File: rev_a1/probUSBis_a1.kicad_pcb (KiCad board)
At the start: 2 copper layers, 23 parts, among them CON1 USB-MINI-B, IC1 ATTINY85-P, P1 USB_A_MALE, P2 CONN_8, P3 CONN_4, U1 LM78L05ACZ

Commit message: made some changes to pcb, added cut edge
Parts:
- moved D4 25.0 mm to (141.0, 111.8), turned to 0 degrees
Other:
- board outline added: 44.5 x 22.9 mm
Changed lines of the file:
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@@
     (links 52)
     (no_connects 52)
-    (area 0 0 0 0)
+    (area 93.996934 87.477599 151.13127 115.23345)
     (thickness 1.6)
-    (drawings 0)
+    (drawings 4)
     (tracks 0)
     (zones 0)
@@
   )
   (module D3 (layer F.Cu)
-    (at 130.81 88.9 180)
+    (at 140.97 111.76)
     (descr "Diode 3 pas")
     (tags "DIODE DEV")
-    (fp_text reference D4 (at 0 0 180) (layer F.SilkS)
-      (effects (font (size 1.016 1.016) (thickness 0.2032)))
-    )
-    (fp_text value DIODE (at 0 0 180) (layer F.SilkS) hide
+    (fp_text reference D4 (at 0 0) (layer F.SilkS)
+      (effects (font (size 1.016 1.016) (thickness 0.2032)))
+    )
+    (fp_text value DIODE (at 0 0) (layer F.SilkS) hide
       (effects (font (size 1.016 1.016) (thickness 0.2032)))
     )
@@
     (fp_line (start 2.54 -1.016) (end 2.54 1.016) (layer F.SilkS) (width 0.3048))
     (fp_line (start 2.286 1.016) (end 2.286 -1.016) (layer F.SilkS) (width 0.3048))
-    (pad 2 thru_hole rect (at 3.81 0 180) (size 1.397 1.397) (drill 0.8128)
+    (pad 2 thru_hole rect (at 3.81 0) (size 1.397 1.397) (drill 0.8128)
       (layers *.Cu *.Mask F.SilkS)
       (net 2 +5V)
     )
-    (pad 1 thru_hole circle (at -3.81 0 180) (size 1.397 1.397) (drill 0.8128)
+    (pad 1 thru_hole circle (at -3.81 0) (size 1.397 1.397) (drill 0.8128)
       (layers *.Cu *.Mask F.SilkS)
       (net 8 N-0000016)
@@
     )
   )
+  (gr_line (start 149.86 91.44) (end 105.41 91.44) (angle 90) (layer Edge.Cuts) (width 0.1))
+  (gr_line (start 149.86 114.3) (end 149.86 91.44) (angle 90) (layer Edge.Cuts) (width 0.1))
+  (gr_line (start 105.41 114.3) (end 149.86 114.3) (angle 90) (layer Edge.Cuts) (width 0.1))
+  (gr_line (start 105.41 91.44) (end 105.41 114.3) (angle 90) (layer Edge.Cuts) (width 0.1))
 )

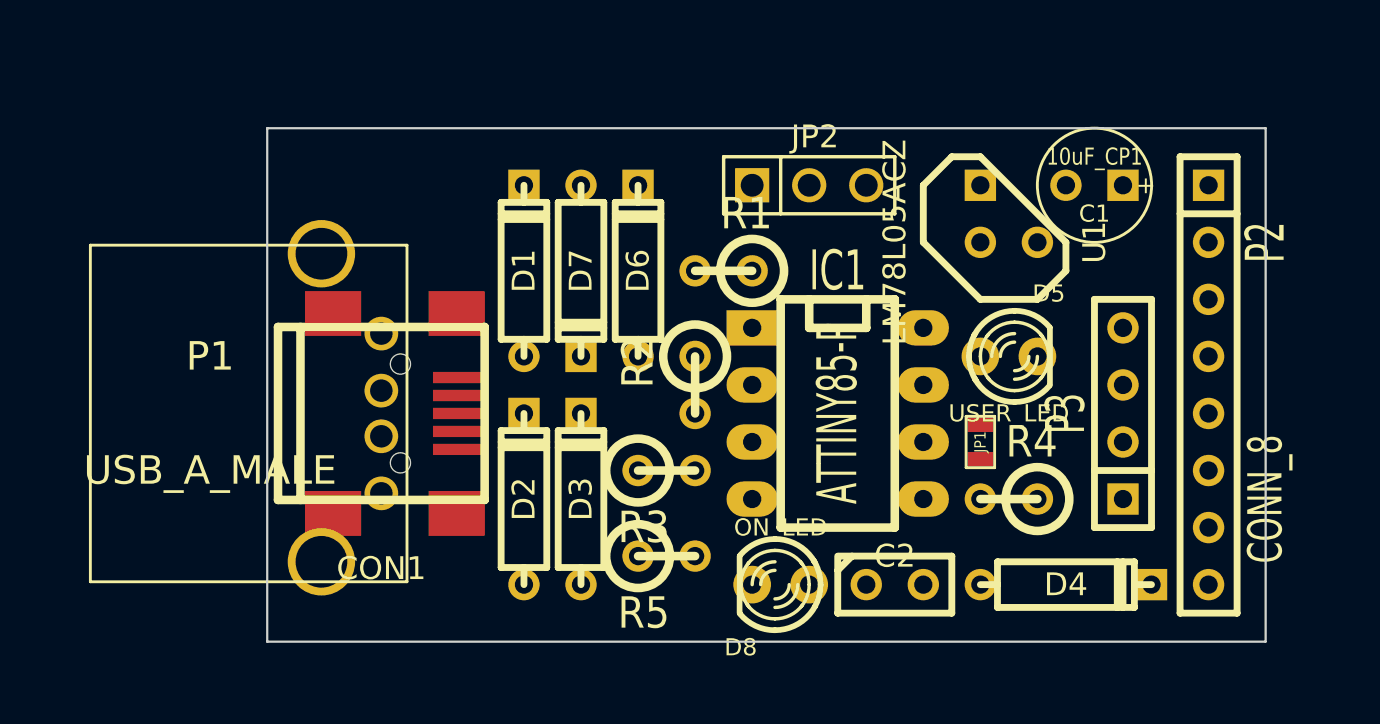
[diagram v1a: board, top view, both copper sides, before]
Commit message: made dsn, also making pin labels
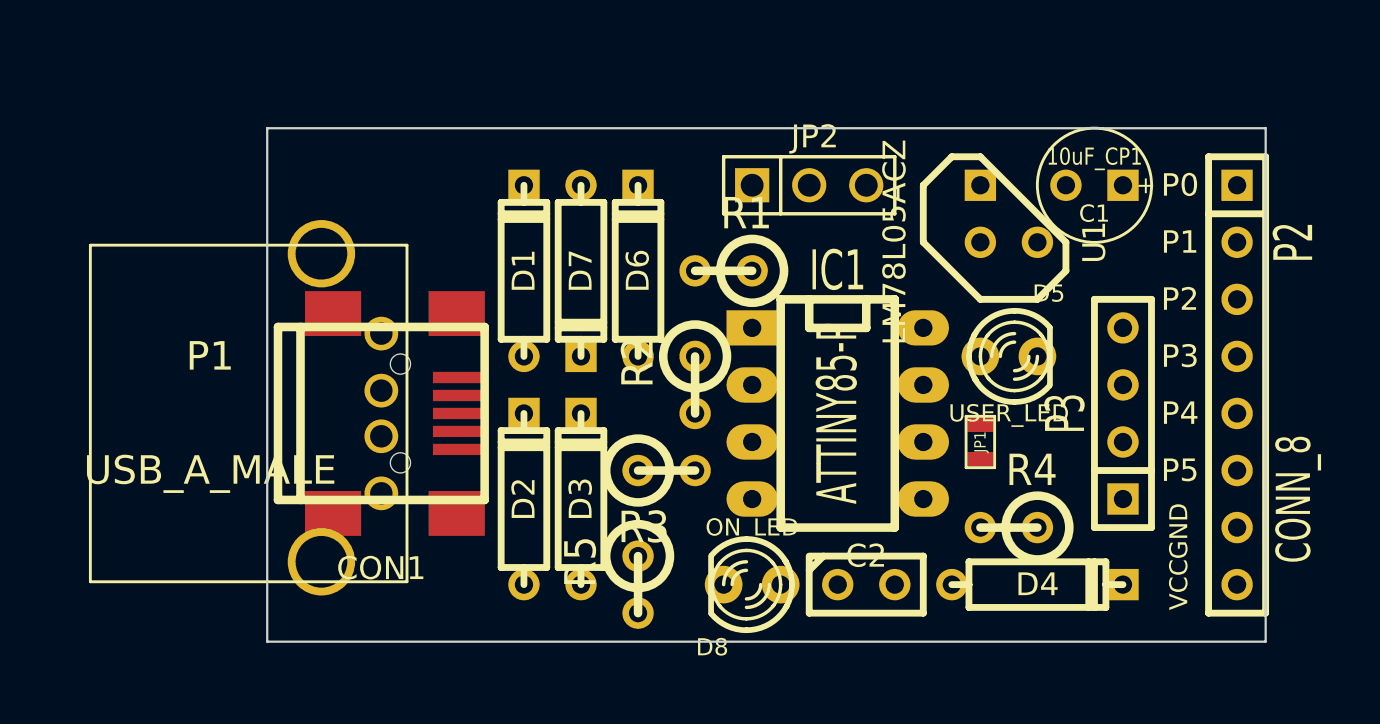
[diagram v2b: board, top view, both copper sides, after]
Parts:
- moved R5 1.80 mm to (121.9, 111.8), turned to 270 degrees
- moved D4 1.27 mm to (139.7, 111.8)
- moved D8 1.27 mm to (127.0, 111.8)
- moved P2 1.27 mm to (148.6, 102.9)
- moved R4 1.27 mm to (138.4, 109.2)
- moved C2 1.27 mm to (132.1, 111.8)
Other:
- board text added: "GND"
- board text added: "P0"
- board text added: "P1"
- board text added: "P2"
- board text added: "P3"
- board text added: "P4"
- board text added: "P5"
- board text added: "VCC"
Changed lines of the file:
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@@
     (links 52)
     (no_connects 52)
-    (area 93.996934 87.477599 151.13127 115.23345)
+    (area 93.996934 90.096623 152.40127 115.23345)
     (thickness 1.6)
-    (drawings 4)
+    (drawings 12)
     (tracks 0)
     (zones 0)
@@
   )
   (module C1 (layer F.Cu)
-    (at 133.35 111.76)
+    (at 132.08 111.76)
     (descr "Condensateur e = 1 pas")
     (tags C)
@@
   )
   (module D3 (layer F.Cu)
-    (at 140.97 111.76)
+    (at 139.7 111.76)
     (descr "Diode 3 pas")
     (tags "DIODE DEV")
@@
   )
   (module LED-3MM (layer F.Cu)
-    (at 128.27 111.76 180)
+    (at 127 111.76 180)
     (descr "LED 3mm - Lead pitch 100mil (2,54mm)")
     (tags "LED led 3mm 3MM 100mil 2,54mm")
@@
   )
   (module SIL-8 (layer F.Cu)
-    (at 147.32 102.87 270)
+    (at 148.59 102.87 270)
     (descr "Connecteur 8 pins")
     (tags "CONN DEV")
@@
   )
   (module R1 (layer F.Cu)
-    (at 138.43 107.95 180)
+    (at 138.43 109.22 180)
     (descr "Resistance verticale")
     (tags R)
@@
   )
   (module R1 (layer F.Cu)
-    (at 123.19 110.49)
+    (at 121.92 111.76 270)
     (descr "Resistance verticale")
     (tags R)
     (autoplace_cost90 10)
     (autoplace_cost180 10)
-    (fp_text reference R5 (at -1.016 2.54) (layer F.SilkS)
+    (fp_text reference R5 (at -1.016 2.54 270) (layer F.SilkS)
       (effects (font (size 1.397 1.27) (thickness 0.2032)))
     )
-    (fp_text value 1K_R (at -1.143 2.54) (layer F.SilkS) hide
+    (fp_text value 1K_R (at -1.143 2.54 270) (layer F.SilkS) hide
       (effects (font (size 1.397 1.27) (thickness 0.2032)))
     )
     (fp_line (start -1.27 0) (end 1.27 0) (layer F.SilkS) (width 0.381))
     (fp_circle (center -1.27 0) (end -0.635 1.27) (layer F.SilkS) (width 0.381))
-    (pad 1 thru_hole circle (at -1.27 0) (size 1.397 1.397) (drill 0.8128)
-      (layers *.Cu *.Mask F.SilkS)
-      (net 3 GND)
-    )
-    (pad 2 thru_hole circle (at 1.27 0) (size 1.397 1.397) (drill 0.8128)
+    (pad 1 thru_hole circle (at -1.27 0 270) (size 1.397 1.397) (drill 0.8128)
+      (layers *.Cu *.Mask F.SilkS)
+      (net 3 GND)
+    )
+    (pad 2 thru_hole circle (at 1.27 0 270) (size 1.397 1.397) (drill 0.8128)
       (layers *.Cu *.Mask F.SilkS)
       (net 18 N-000009)
@@
     )
   )
+  (gr_text VCC (at 146 111.76 90) (layer F.SilkS)
+    (effects (font (size 0.8 0.8) (thickness 0.1)))
+  )
+  (gr_text "   GND" (at 146 109.9 90) (layer F.SilkS)
+    (effects (font (size 0.8 0.8) (thickness 0.1)))
+  )
+  (gr_text P5 (at 146.05 106.68) (layer F.SilkS)
+    (effects (font (size 1 1) (thickness 0.25)))
+  )
+  (gr_text P4 (at 146.05 104.14) (layer F.SilkS)
+    (effects (font (size 1 1) (thickness 0.25)))
+  )
+  (gr_text P3 (at 146.05 101.6) (layer F.SilkS)
+    (effects (font (size 1 1) (thickness 0.25)))
+  )
+  (gr_text P1 (at 146.05 96.52) (layer F.SilkS)
+    (effects (font (size 1 1) (thickness 0.25)))
+  )
+  (gr_text P2 (at 146.05 99.06) (layer F.SilkS)
+    (effects (font (size 1 1) (thickness 0.25)))
+  )
+  (gr_text P0 (at 146.05 93.98) (layer F.SilkS)
+    (effects (font (size 1 1) (thickness 0.25)))
+  )
   (gr_line (start 149.86 91.44) (end 105.41 91.44) (angle 90) (layer Edge.Cuts) (width 0.1))

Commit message: editing pcb layout, trying to compress more
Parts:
- moved D4 17.0 mm to (130.5, 97.5), turned to 180 degrees
- moved R4 11.0 mm to (142.6, 99.1), turned to 90 degrees
- moved P3 8.52 mm to (139.7, 111.8), turned to 0 degrees
- moved P1 2.64 mm to (111.2, 106.7)
- moved JP2 2.54 mm to (127.0, 94.0)
- moved U1 1.80 mm to (137.2, 94.0)
- moved D5 1.62 mm to (138.7, 100.0)
- moved D8 1.50 mm to (125.5, 111.8), turned to 270 degrees
- moved C2 1.48 mm to (130.6, 111.8)
- moved R1 1.29 mm to (124.5, 98.0), turned to 270 degrees
- moved JP1 1.27 mm to (137.2, 104.1)
- moved R3 1.27 mm to (121.9, 106.7), turned to 270 degrees
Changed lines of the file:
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@@
   )
   (module C1 (layer F.Cu)
-    (at 132.08 111.76)
+    (at 130.6 111.76)
     (descr "Condensateur e = 1 pas")
     (tags C)
@@
   )
   (module D3 (layer F.Cu)
-    (at 139.7 111.76)
+    (at 130.5 97.5 180)
     (descr "Diode 3 pas")
     (tags "DIODE DEV")
-    (fp_text reference D4 (at 0 0) (layer F.SilkS)
-      (effects (font (size 1.016 1.016) (thickness 0.2032)))
-    )
-    (fp_text value DIODE (at 0 0) (layer F.SilkS) hide
+    (fp_text reference D4 (at 0 0 180) (layer F.SilkS)
+      (effects (font (size 1.016 1.016) (thickness 0.2032)))
+    )
+    (fp_text value DIODE (at 0 0 180) (layer F.SilkS) hide
       (effects (font (size 1.016 1.016) (thickness 0.2032)))
     )
@@
     (fp_line (start 2.54 -1.016) (end 2.54 1.016) (layer F.SilkS) (width 0.3048))
     (fp_line (start 2.286 1.016) (end 2.286 -1.016) (layer F.SilkS) (width 0.3048))
-    (pad 2 thru_hole rect (at 3.81 0) (size 1.397 1.397) (drill 0.8128)
+    (pad 2 thru_hole rect (at 3.81 0 180) (size 1.397 1.397) (drill 0.8128)
       (layers *.Cu *.Mask F.SilkS)
       (net 2 +5V)
     )
-    (pad 1 thru_hole circle (at -3.81 0) (size 1.397 1.397) (drill 0.8128)
+    (pad 1 thru_hole circle (at -3.81 0 180) (size 1.397 1.397) (drill 0.8128)
       (layers *.Cu *.Mask F.SilkS)
       (net 8 N-0000016)
@@
   )
   (module LED-3MM (layer F.Cu)
-    (at 138.43 101.6)
+    (at 138.7 100)
     (descr "LED 3mm - Lead pitch 100mil (2,54mm)")
     (tags "LED led 3mm 3MM 100mil 2,54mm")
@@
   )
   (module LED-3MM (layer F.Cu)
-    (at 127 111.76 180)
+    (at 125.5 111.76 270)
     (descr "LED 3mm - Lead pitch 100mil (2,54mm)")
     (tags "LED led 3mm 3MM 100mil 2,54mm")
-    (fp_text reference D8 (at 1.778 -2.794 180) (layer F.SilkS)
+    (fp_text reference D8 (at 1.778 -2.794 270) (layer F.SilkS)
       (effects (font (size 0.762 0.762) (thickness 0.0889)))
     )
-    (fp_text value ON_LED (at 0 2.54 180) (layer F.SilkS)
+    (fp_text value ON_LED (at 0 2.54 270) (layer F.SilkS)
       (effects (font (size 0.762 0.762) (thickness 0.0889)))
     )
@@
     (fp_arc (start 0.254 0) (end -1.778 0) (angle 28.3) (layer F.SilkS) (width 0.254))
     (fp_arc (start 0.254 0) (end -1.47574 1.06426) (angle 31.6) (layer F.SilkS) (width 0.254))
-    (pad 1 thru_hole circle (at -1.27 0 180) (size 1.6764 1.6764) (drill 0.8128)
+    (pad 1 thru_hole circle (at -1.27 0 270) (size 1.6764 1.6764) (drill 0.8128)
       (layers *.Cu *.Mask F.SilkS)
       (net 19 VCC)
     )
-    (pad 2 thru_hole circle (at 1.27 0 180) (size 1.6764 1.6764) (drill 0.8128)
+    (pad 2 thru_hole circle (at 1.27 0 270) (size 1.6764 1.6764) (drill 0.8128)
       (layers *.Cu *.Mask F.SilkS)
       (net 18 N-000009)
@@
   )
   (module PIN_ARRAY_3X1 (layer F.Cu)
-    (at 129.54 93.98)
+    (at 127 93.98)
     (descr "Connecteur 3 pins")
     (tags "CONN DEV")
@@
   )
   (module USB_A (layer F.Cu)
-    (at 110.49 104.14 180)
+    (at 111.2 106.68 180)
     (fp_text reference P1 (at 7.62 2.54 180) (layer F.SilkS)
       (effects (font (thickness 0.3048)))
@@
   )
   (module SIL-4 (layer F.Cu)
-    (at 143.51 104.14 90)
+    (at 139.7 111.76)
     (descr "Connecteur 4 pibs")
     (tags "CONN DEV")
-    (fp_text reference P3 (at 0 -2.54 90) (layer F.SilkS)
+    (fp_text reference P3 (at 0 -2.54) (layer F.SilkS)
       (effects (font (size 1.73482 1.08712) (thickness 0.3048)))
     )
-    (fp_text value CONN_4 (at 0 -2.54 90) (layer F.SilkS) hide
+    (fp_text value CONN_4 (at 0 -2.54) (layer F.SilkS) hide
       (effects (font (size 1.524 1.016) (thickness 0.3048)))
     )
@@
     (fp_line (start 5.08 1.27) (end -5.08 1.27) (layer F.SilkS) (width 0.3048))
     (fp_line (start -2.54 1.27) (end -2.54 -1.27) (layer F.SilkS) (width 0.3048))
-    (pad 1 thru_hole rect (at -3.81 0 90) (size 1.397 1.397) (drill 0.8128)
+    (pad 1 thru_hole rect (at -3.81 0) (size 1.397 1.397) (drill 0.8128)
       (layers *.Cu *.Mask F.SilkS)
       (net 1 +3.3V)
     )
-    (pad 2 thru_hole circle (at -1.27 0 90) (size 1.397 1.397) (drill 0.8128)
+    (pad 2 thru_hole circle (at -1.27 0) (size 1.397 1.397) (drill 0.8128)
       (layers *.Cu *.Mask F.SilkS)
       (net 2 +5V)
     )
-    (pad 3 thru_hole circle (at 1.27 0 90) (size 1.397 1.397) (drill 0.8128)
-      (layers *.Cu *.Mask F.SilkS)
-      (net 3 GND)
-    )
-    (pad 4 thru_hole circle (at 3.81 0 90) (size 1.397 1.397) (drill 0.8128)
+    (pad 3 thru_hole circle (at 1.27 0) (size 1.397 1.397) (drill 0.8128)
+      (layers *.Cu *.Mask F.SilkS)
+      (net 3 GND)
+    )
+    (pad 4 thru_hole circle (at 3.81 0) (size 1.397 1.397) (drill 0.8128)
       (layers *.Cu *.Mask F.SilkS)
       (net 20 VIN)
@@
   )
   (module R1 (layer F.Cu)
-    (at 125.73 97.79 180)
+    (at 124.46 98 270)
     (descr "Resistance verticale")
     (tags R)
     (autoplace_cost90 10)
     (autoplace_cost180 10)
-    (fp_text reference R1 (at -1.016 2.54 180) (layer F.SilkS)
-      (effects (font (size 1.397 1.27) (thickness 0.2032)))
-    )
-    (fp_text value 1.5K_R (at -1.143 2.54 180) (layer F.SilkS) hide
+    (fp_text reference R1 (at -1.016 2.54 270) (layer F.SilkS)
+      (effects (font (size 1.397 1.27) (thickness 0.2032)))
+    )
+    (fp_text value 1.5K_R (at -1.143 2.54 270) (layer F.SilkS) hide
       (effects (font (size 1.397 1.27) (thickness 0.2032)))
     )
     (fp_line (start -1.27 0) (end 1.27 0) (layer F.SilkS) (width 0.381))
     (fp_circle (center -1.27 0) (end -0.635 1.27) (layer F.SilkS) (width 0.381))
-    (pad 1 thru_hole circle (at -1.27 0 180) (size 1.397 1.397) (drill 0.8128)
+    (pad 1 thru_hole circle (at -1.27 0 270) (size 1.397 1.397) (drill 0.8128)
       (layers *.Cu *.Mask F.SilkS)
       (net 19 VCC)
     )
-    (pad 2 thru_hole circle (at 1.27 0 180) (size 1.397 1.397) (drill 0.8128)
+    (pad 2 thru_hole circle (at 1.27 0 270) (size 1.397 1.397) (drill 0.8128)
       (layers *.Cu *.Mask F.SilkS)
       (net 11 N-0000019)
@@
   )
   (module R1 (layer F.Cu)
-    (at 123.19 106.68)
+    (at 121.92 106.68 270)
     (descr "Resistance verticale")
     (tags R)
     (autoplace_cost90 10)
     (autoplace_cost180 10)
-    (fp_text reference R3 (at -1.016 2.54) (layer F.SilkS)
-      (effects (font (size 1.397 1.27) (thickness 0.2032)))
-    )
-    (fp_text value 68R (at -1.143 2.54) (layer F.SilkS) hide
+    (fp_text reference R3 (at -1.016 2.54 270) (layer F.SilkS)
+      (effects (font (size 1.397 1.27) (thickness 0.2032)))
+    )
+    (fp_text value 68R (at -1.143 2.54 270) (layer F.SilkS) hide
       (effects (font (size 1.397 1.27) (thickness 0.2032)))
     )
     (fp_line (start -1.27 0) (end 1.27 0) (layer F.SilkS) (width 0.381))
     (fp_circle (center -1.27 0) (end -0.635 1.27) (layer F.SilkS) (width 0.381))
-    (pad 1 thru_hole circle (at -1.27 0) (size 1.397 1.397) (drill 0.8128)
+    (pad 1 thru_hole circle (at -1.27 0 270) (size 1.397 1.397) (drill 0.8128)
       (layers *.Cu *.Mask F.SilkS)
       (net 9 N-0000017)
     )
-    (pad 2 thru_hole circle (at 1.27 0) (size 1.397 1.397) (drill 0.8128)
+    (pad 2 thru_hole circle (at 1.27 0 270) (size 1.397 1.397) (drill 0.8128)
       (layers *.Cu *.Mask F.SilkS)
       (net 7 N-0000015)
@@
   )
   (module R1 (layer F.Cu)
-    (at 138.43 109.22 180)
+    (at 142.6 99.06 90)
     (descr "Resistance verticale")
     (tags R)
     (autoplace_cost90 10)
     (autoplace_cost180 10)
-    (fp_text reference R4 (at -1.016 2.54 180) (layer F.SilkS)
-      (effects (font (size 1.397 1.27) (thickness 0.2032)))
-    )
-    (fp_text value 1K_R (at -1.143 2.54 180) (layer F.SilkS) hide
+    (fp_text reference R4 (at -1.016 2.54 90) (layer F.SilkS)
+      (effects (font (size 1.397 1.27) (thickness 0.2032)))
+    )
+    (fp_text value 1K_R (at -1.143 2.54 90) (layer F.SilkS) hide
       (effects (font (size 1.397 1.27) (thickness 0.2032)))
     )
     (fp_line (start -1.27 0) (end 1.27 0) (layer F.SilkS) (width 0.381))
     (fp_circle (center -1.27 0) (end -0.635 1.27) (layer F.SilkS) (width 0.381))
-    (pad 1 thru_hole circle (at -1.27 0 180) (size 1.397 1.397) (drill 0.8128)
+    (pad 1 thru_hole circle (at -1.27 0 90) (size 1.397 1.397) (drill 0.8128)
       (layers *.Cu *.Mask F.SilkS)
       (net 5 N-0000011)
     )
-    (pad 2 thru_hole circle (at 1.27 0 180) (size 1.397 1.397) (drill 0.8128)
+    (pad 2 thru_hole circle (at 1.27 0 90) (size 1.397 1.397) (drill 0.8128)
       (layers *.Cu *.Mask F.SilkS)
       (net 3 GND)
@@
   )
   (module TO92-123 (layer F.Cu)
-    (at 138.43 95.25 90)
+    (at 137.16 93.98 90)
     (descr "Transistor TO92 brochage type BC237")
     (tags "TR TO92")
@@
   )
   (module SM0603 (layer F.Cu)
-    (at 137.16 105.41 90)
+    (at 137.16 104.14 90)
     (attr smd)
     (fp_text reference JP1 (at 0 0 90) (layer F.SilkS)
